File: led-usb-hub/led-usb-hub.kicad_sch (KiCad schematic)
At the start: 142 parts, among them J1 USBC_USB2.0, J2 RGBUSB_54-00266, J3 RGBUSB_54-00266, J4 RGBUSB_54-00266, J5 SWD, SW1 RESET, SW2 BOOLSEL, SW3 LED EN, U1 RP2040, U10 TPD2EUSB30, U11 TPD2EUSB30, U12 TC54VN3002, U13 W25Q16JVSN, U2 TPS2042D, U3 TPS2042D, U4 TPS563257DRLR, U5 TPS563257DRLR, U6 TUSB2046IBVF, U7 TPD2EUSB30, U8 TPD2EUSB30, U9 TPD2EUSB30, Y1 12Mhz, Y2 6Mhz

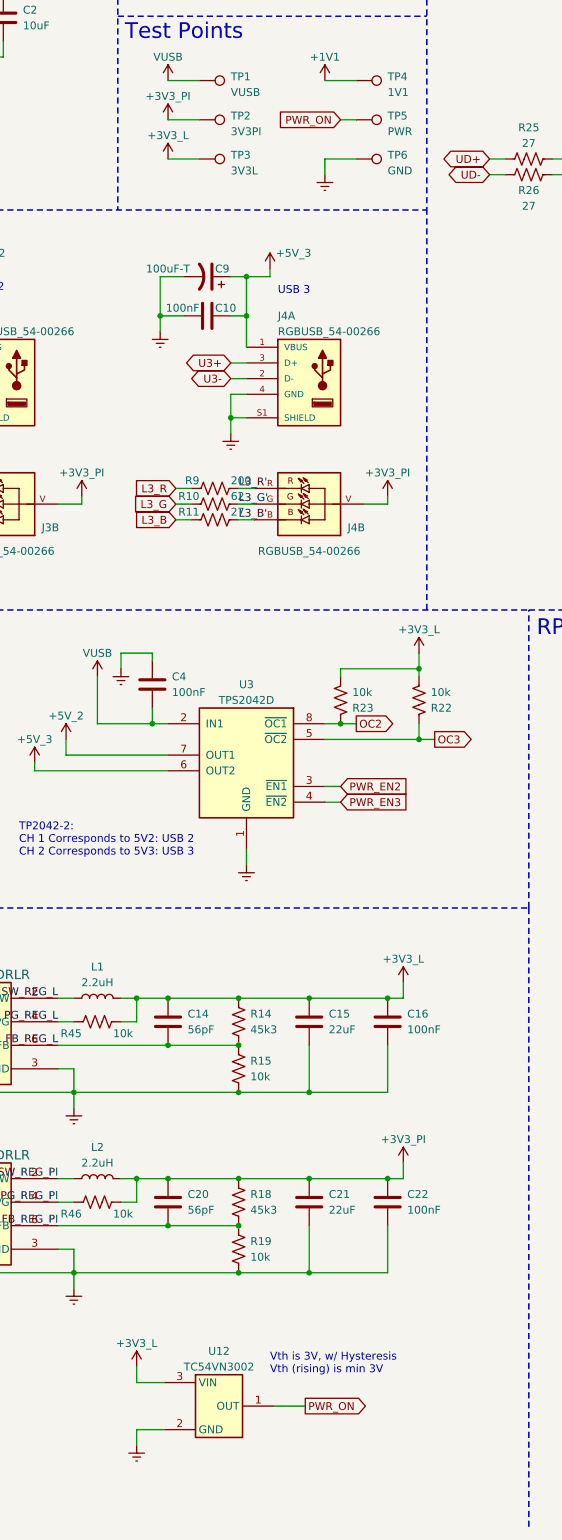
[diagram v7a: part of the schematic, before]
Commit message: Remove Power-On Monitor, was causing issues with device booting Switch to using a MAX809T for future revisions
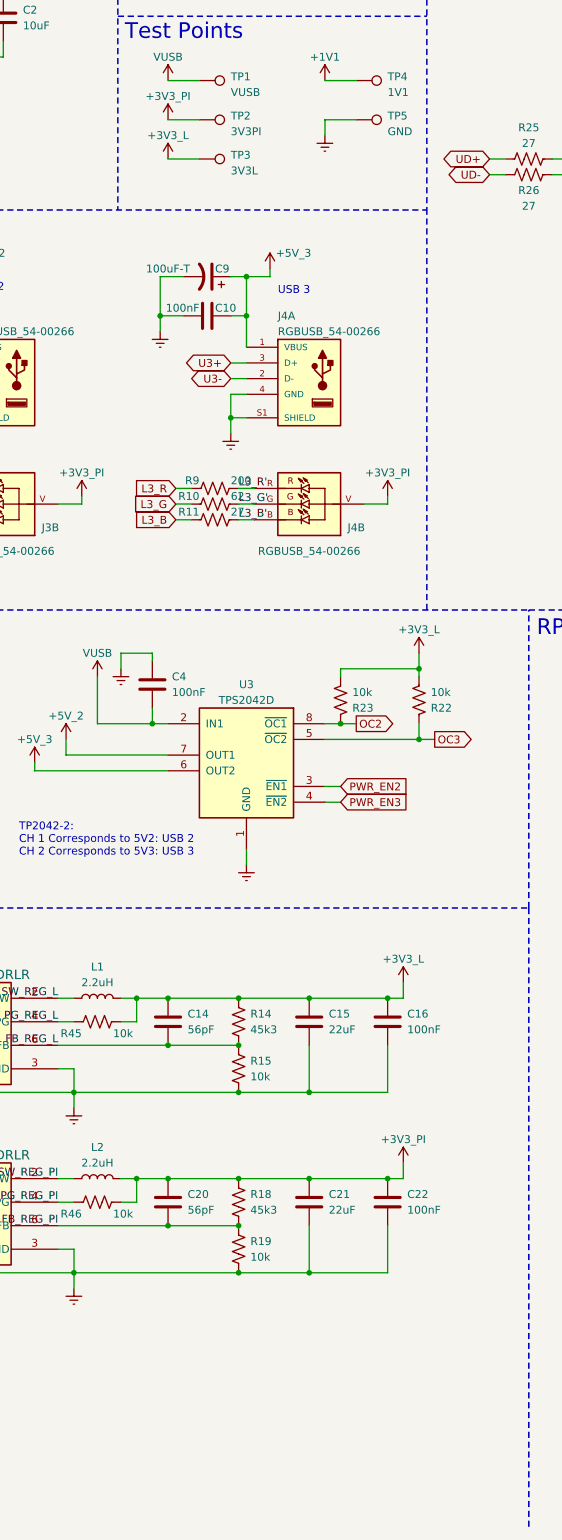
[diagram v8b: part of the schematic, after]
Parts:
- removed TP5: PWR, TestPoint:TestPoint_Pad_1.0x1.0mm_Mod, symbol Connector:TestPoint
- removed U12: TC54VN3002, Package_TO_SOT_SMD:SOT-23, symbol TC54VN:TC54VN3002
- renumbered TP6 to TP5
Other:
- note removed: "Vth is 3V, w/ Hysteresis Vth (rising) is min 3V"
- moved on the sheet: TP5
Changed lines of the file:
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@@
     (stroke (width 0) (type default))
   )
-  (wire (pts (xy 113.03 261.62) (xy 113.03 259.08))
-    (stroke (width 0) (type default))
-  )
   (polyline (pts (xy 337.82 179.705) (xy 407.924 179.705))
     (stroke (width 0.25) (type dash))
@@
     (stroke (width 0) (type default))
   )
-  (wire (pts (xy 143.51 63.5) (xy 143.51 66.04))
+  (wire (pts (xy 143.51 57.15) (xy 143.51 59.69))
     (stroke (width 0) (type default))
   )
@@
     (stroke (width 0) (type default))
   )
-  (wire (pts (xy 143.51 63.5) (xy 148.59 63.5))
+  (wire (pts (xy 143.51 57.15) (xy 148.59 57.15))
     (stroke (width 0) (type default))
   )
@@
     (stroke (width 0) (type default))
   )
-  (wire (pts (xy 140.335 265.43) (xy 135.255 265.43))
-    (stroke (width 0) (type default))
-  )
   (wire (pts (xy 328.93 58.42) (xy 328.93 38.1))
     (stroke (width 0) (type default))
@@
     (stroke (width 0) (type default))
   )
-  (wire (pts (xy 113.03 269.24) (xy 117.475 269.24))
-    (stroke (width 0) (type default))
-  )
   (wire (pts (xy 158.75 146.05) (xy 158.75 147.32))
     (stroke (width 0) (type default))
@@
     (stroke (width 0) (type default))
   )
-  (wire (pts (xy 146.05 57.15) (xy 148.59 57.15))
-    (stroke (width 0) (type default))
-  )
   (wire (pts (xy 363.22 243.84) (xy 365.76 243.84))
     (stroke (width 0) (type default))
@@
     (stroke (width 0) (type default))
   )
-  (wire (pts (xy 113.03 261.62) (xy 117.475 261.62))
-    (stroke (width 0) (type default))
-  )
   (wire (pts (xy 345.44 104.14) (xy 342.9 104.14))
     (stroke (width 0) (type default))
@@
     (stroke (width 0) (type default))
   )
-  (wire (pts (xy 113.03 269.24) (xy 113.03 271.78))
-    (stroke (width 0) (type default))
-  )
   (wire (pts (xy 335.28 88.9) (xy 335.28 113.03))
     (stroke (width 0) (type default))
@@
     (effects (font (size 1.27 1.27)) (justify left bottom))
   )
-  (text "Vth is 3V, w/ Hysteresis\nVth (rising) is min 3V" (at 134.62 260.35 0)
-    (effects (font (size 1.27 1.27)) (justify left bottom))
-  )
   (text "CL = 2 * (C_Load - C_Stray)\nCL = 2 * (16 - ~5)\nCL ~= 22pF\n\nR_Ext = 1 / (2*π*F*CL)\nR_Ext = 604"
     (at 207.645 266.7 0)
@@
     )
   )
-  (global_label "PWR_ON" (shape input) (at 146.05 57.15 180) (fields_autoplaced)
-    (effects (font (size 1.27 1.27)) (justify right))
-    (property "Intersheetrefs" "${INTERSHEET_REFS}" (at 135.5242 57.15 0)
-      (effects (font (size 1.27 1.27)) (justify right) hide)
-    )
-  )
   (global_label "RESET" (shape input) (at 228.6 190.5 180) (fields_autoplaced)
     (effects (font (size 1.27 1.27)) (justify right))
@@
     )
   )
-  (global_label "PWR_ON" (shape output) (at 140.335 265.43 0) (fields_autoplaced)
-    (effects (font (size 1.27 1.27)) (justify left))
-    (property "Intersheetrefs" "${INTERSHEET_REFS}" (at 150.8608 265.43 0)
-      (effects (font (size 1.27 1.27)) (justify left) hide)
-    )
-  )
   (global_label "U2+" (shape bidirectional) (at 78.74 96.52 180) (fields_autoplaced)
     (effects (font (size 1.27 1.27)) (justify right))
@@
     )
   )
-  (symbol (lib_id "Connector:TestPoint") (at 148.59 63.5 270) (unit 1)
+  (symbol (lib_id "Connector:TestPoint") (at 148.59 57.15 270) (unit 1)
     (in_bom yes) (on_board yes) (dnp no) (fields_autoplaced)
-    (property "Reference" "TP6" (at 153.67 62.865 90)
+    (property "Reference" "TP5" (at 153.67 56.515 90)
       (effects (font (size 1.27 1.27)) (justify left))
     )
-    (property "Value" "GND" (at 153.67 65.405 90)
+    (property "Value" "GND" (at 153.67 59.055 90)
       (effects (font (size 1.27 1.27)) (justify left))
     )
-    (property "Footprint" "TestPoint:TestPoint_Pad_1.0x1.0mm_Mod" (at 148.59 68.58 0)
+    (property "Footprint" "TestPoint:TestPoint_Pad_1.0x1.0mm_Mod" (at 148.59 62.23 0)
       (effects (font (size 1.27 1.27)) hide)
     )
-    (property "Datasheet" "~" (at 148.59 68.58 0)
+    (property "Datasheet" "~" (at 148.59 62.23 0)
       (effects (font (size 1.27 1.27)) hide)
     )
@@
       (project "led-usb-hub"
         (path "/872229b5-49ea-4e15-b82a-ed1f213c1d75"
-          (reference "TP6") (unit 1)
+          (reference "TP5") (unit 1)
         )
       )
@@
     )
   )
-  (symbol (lib_id "power:Earth") (at 113.03 271.78 0) (mirror y) (unit 1)
-    (in_bom yes) (on_board yes) (dnp no) (fields_autoplaced)
-    (property "Reference" "#PWR038" (at 113.03 278.13 0)
-      (effects (font (size 1.27 1.27)) hide)
-    )
-    (property "Value" "Earth" (at 113.03 275.59 0)
-      (effects (font (size 1.27 1.27)) hide)
-    )
-    (property "Footprint" "" (at 113.03 271.78 0)
-      (effects (font (size 1.27 1.27)) hide)
-    )
-    (property "Datasheet" "~" (at 113.03 271.78 0)
-      (effects (font (size 1.27 1.27)) hide)
-    )
-    (pin "1")
-    (instances
-      (project "led-usb-hub"
-        (path "/872229b5-49ea-4e15-b82a-ed1f213c1d75"
-          (reference "#PWR038") (unit 1)
-        )
-      )
-    )
-  )
   (symbol (lib_id "Device:R_US") (at 67.31 203.2 0) (unit 1)
     (in_bom yes) (on_board yes) (dnp no)
@@
     )
   )
-  (symbol (lib_id "Connector:TestPoint") (at 148.59 57.15 270) (unit 1)
-    (in_bom yes) (on_board yes) (dnp no) (fields_autoplaced)
-    (property "Reference" "TP5" (at 153.67 56.515 90)
-      (effects (font (size 1.27 1.27)) (justify left))
-    )
-    (property "Value" "PWR" (at 153.67 59.055 90)
-      (effects (font (size 1.27 1.27)) (justify left))
-    )
-    (property "Footprint" "TestPoint:TestPoint_Pad_1.0x1.0mm_Mod" (at 148.59 62.23 0)
-      (effects (font (size 1.27 1.27)) hide)
-    )
-    (property "Datasheet" "~" (at 148.59 62.23 0)
-      (effects (font (size 1.27 1.27)) hide)
-    )
-    (pin "1")
-    (instances
-      (project "led-usb-hub"
-        (path "/872229b5-49ea-4e15-b82a-ed1f213c1d75"
-          (reference "TP5") (unit 1)
-        )
-      )
-    )
-  )
   (symbol (lib_id "TPD2EUSB30DRTR:TPD2EUSB30") (at 393.7 104.14 0) (mirror y) (unit 1)
     (in_bom yes) (on_board yes) (dnp no)
@@
     )
   )
-  (symbol (lib_id "power:Earth") (at 143.51 66.04 0) (unit 1)
+  (symbol (lib_id "power:Earth") (at 143.51 59.69 0) (unit 1)
     (in_bom yes) (on_board yes) (dnp no) (fields_autoplaced)
-    (property "Reference" "#PWR047" (at 143.51 72.39 0)
+    (property "Reference" "#PWR047" (at 143.51 66.04 0)
       (effects (font (size 1.27 1.27)) hide)
     )
-    (property "Value" "Earth" (at 143.51 69.85 0)
+    (property "Value" "Earth" (at 143.51 63.5 0)
       (effects (font (size 1.27 1.27)) hide)
     )
-    (property "Footprint" "" (at 143.51 66.04 0)
+    (property "Footprint" "" (at 143.51 59.69 0)
       (effects (font (size 1.27 1.27)) hide)
     )
-    (property "Datasheet" "~" (at 143.51 66.04 0)
+    (property "Datasheet" "~" (at 143.51 59.69 0)
       (effects (font (size 1.27 1.27)) hide)
     )
@@
     )
   )
-  (symbol (lib_id "power:+3V3_L") (at 113.03 259.08 0) (unit 1)
-    (in_bom yes) (on_board yes) (dnp no) (fields_autoplaced)
-    (property "Reference" "#PWR059" (at 113.03 262.89 0)
-      (effects (font (size 1.27 1.27)) hide)
-    )
-    (property "Value" "+3V3_L" (at 113.03 255.27 0)
-      (effects (font (size 1.27 1.27)))
-    )
-    (property "Footprint" "" (at 113.03 259.08 0)
-      (effects (font (size 1.27 1.27)) hide)
-    )
-    (property "Datasheet" "" (at 113.03 259.08 0)
-      (effects (font (size 1.27 1.27)) hide)
-    )
-    (pin "1")
-    (instances
-      (project "led-usb-hub"
-        (path "/872229b5-49ea-4e15-b82a-ed1f213c1d75"
-          (reference "#PWR059") (unit 1)
-        )
-      )
-    )
-  )
   (symbol (lib_id "Device:R_US") (at 71.12 40.64 180) (unit 1)
     (in_bom yes) (on_board yes) (dnp no)
@@
         )
       )
-    )
-  )
-  (symbol (lib_id "TC54VN:TC54VN3002") (at 126.365 257.81 0) (unit 1)
-    (in_bom yes) (on_board yes) (dnp no) (fields_autoplaced)
-    (property "Reference" "U12" (at 126.365 256.54 0)
-      (effects (font (size 1.27 1.27)))
-    )
-    (property "Value" "TC54VN3002" (at 126.365 259.08 0)
-      (effects (font (size 1.27 1.27)))
-    )
-    (property "Footprint" "Package_TO_SOT_SMD:SOT-23" (at 126.365 257.81 0)
-      (effects (font (size 1.27 1.27)) hide)
-    )
-    (property "Datasheet" "" (at 126.365 257.81 0)
-      (effects (font (size 1.27 1.27)) hide)
-    )
-    (pin "1")
-    (pin "2")
-    (pin "3")
-    (instances
-      (project "led-usb-hub"
-        (path "/872229b5-49ea-4e15-b82a-ed1f213c1d75"
-          (reference "U12") (unit 1)
-        )
-      )
